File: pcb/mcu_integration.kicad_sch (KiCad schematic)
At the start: 32 parts, among them J5 DM3BT-DSF-PEJS, M1 MountingHole_Pad, M2 MountingHole_Pad, M3 MountingHole_Pad, M4 MountingHole_Pad, U1 STM32F103RBTx, U6 LM35DM, Y1 ECS-80-18-5PX-GM-TR

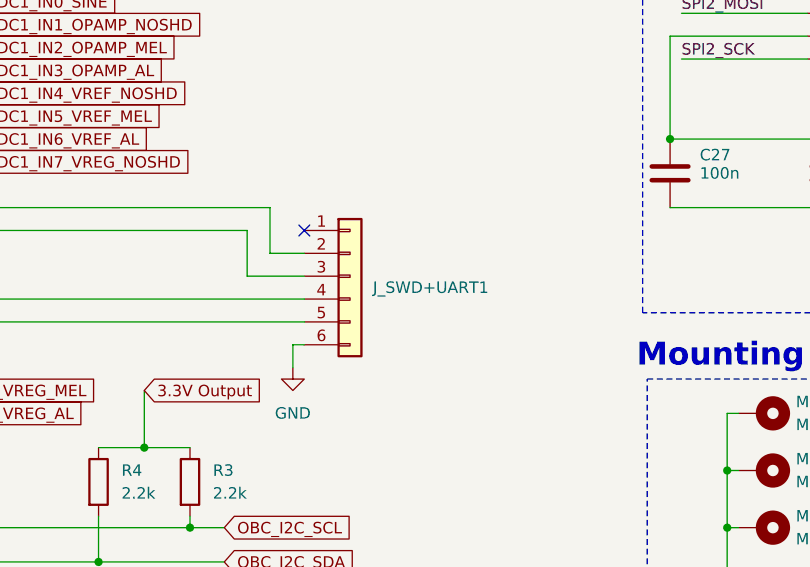
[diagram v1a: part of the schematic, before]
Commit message: Increased board size from 5x5 to 7x7
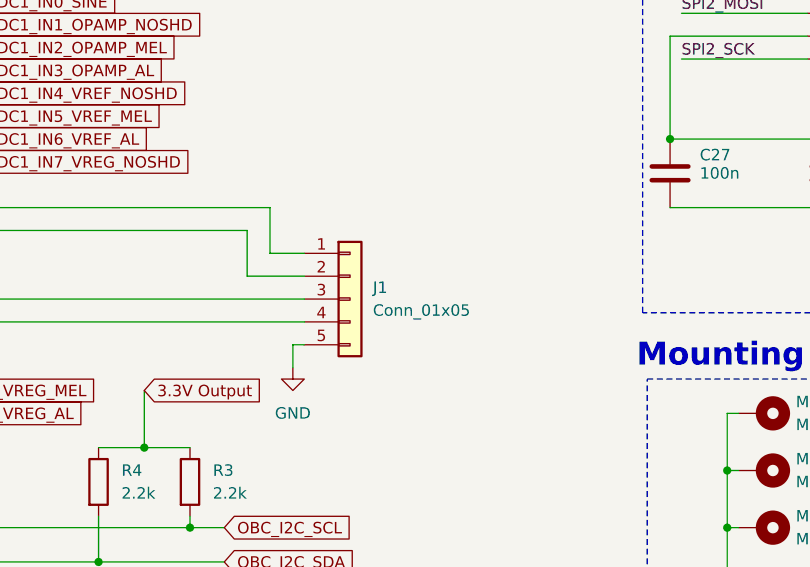
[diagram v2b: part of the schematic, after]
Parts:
- removed J_SWD+UART1: Conn_01x06, Connector_PinHeader_2.54mm:PinHeader_1x06_P2.54mm_Vertical, symbol Connector_Generic:Conn_01x06
- added J1: Conn_01x05, Connector_PinHeader_2.54mm:PinHeader_1x05_P2.54mm_Vertical, symbol Connector_Generic:Conn_01x05
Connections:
- net GND: now also J1.5 (Pin_5)
- net SWCLK: now also J1.4 (Pin_4)
- net SWDIO: now also J1.3 (Pin_3)
- net USART1_RX: now also J1.2 (Pin_2)
- net USART1_TX: now also J1.1 (Pin_1)
- no-connect marks 31 -> 30
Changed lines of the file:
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@@
 	)
 	(no_connect
-		(at 163.83 62.23)
-	)
-	(no_connect
 		(at 116.84 105.41)
 	)
@@
 	(label "SPI2_SCK"
 		(at 205.74 43.18 0)
+		(fields_autoplaced yes)
 		(effects
 			(font
@@
 	(label "SPI2_CS_NSS"
 		(at 205.74 35.56 0)
+		(fields_autoplaced yes)
 		(effects
 			(font
@@
 	(label "HSE_OSC_OUT"
 		(at 67.31 49.53 0)
+		(fields_autoplaced yes)
 		(effects
 			(font
@@
 	(label "USART1_TX"
 		(at 119.38 59.69 0)
+		(fields_autoplaced yes)
 		(effects
 			(font
@@
 	(label "HSE_OSC_IN"
 		(at 67.31 46.99 0)
+		(fields_autoplaced yes)
 		(effects
 			(font
@@
 	(label "SPI2_CS_NSS"
 		(at 119.38 110.49 0)
+		(fields_autoplaced yes)
 		(effects
 			(font
@@
 	(label "SPI2_MOSI"
 		(at 205.74 38.1 0)
+		(fields_autoplaced yes)
 		(effects
 			(font
@@
 	(label "SPI2_MOSI"
 		(at 119.38 118.11 0)
+		(fields_autoplaced yes)
 		(effects
 			(font
@@
 	(label "SPI2_MISO"
 		(at 119.38 115.57 0)
+		(fields_autoplaced yes)
 		(effects
 			(font
@@
 	(label "SWCLK"
 		(at 119.38 72.39 0)
+		(fields_autoplaced yes)
 		(effects
 			(font
@@
 	(label "USART1_RX"
 		(at 119.38 62.23 0)
+		(fields_autoplaced yes)
 		(effects
 			(font
@@
 	(label "SPI2_MISO"
 		(at 276.86 40.64 180)
+		(fields_autoplaced yes)
 		(effects
 			(font
@@
 	(label "BOOT0"
 		(at 68.58 40.64 0)
+		(fields_autoplaced yes)
 		(effects
 			(font
@@
 	(label "NRST"
 		(at 73.66 36.83 0)
+		(fields_autoplaced yes)
 		(effects
 			(font
@@
 	(label "SWDIO"
 		(at 119.38 69.85 0)
+		(fields_autoplaced yes)
 		(effects
 			(font
@@
 	(label "SPI2_SCK"
 		(at 119.38 113.03 0)
+		(fields_autoplaced yes)
 		(effects
 			(font
@@
 	)
 	(symbol
-		(lib_id "Connector_Generic:Conn_01x06")
-		(at 168.91 67.31 0)
-		(unit 1)
-		(exclude_from_sim no)
-		(in_bom yes)
-		(on_board yes)
-		(dnp no)
-		(fields_autoplaced yes)
-		(property "Reference" "J_SWD+UART1"
-			(at 171.45 68.58 0)
-			(effects
-				(font
-					(size 1.27 1.27)
-				)
-				(justify left)
-			)
-		)
-		(property "Value" "Conn_01x06"
-			(at 171.45 69.85 0)
-			(effects
-				(font
-					(size 1.27 1.27)
-				)
-				(justify left)
-				(hide yes)
-			)
-		)
-		(property "Footprint" "Connector_PinHeader_2.54mm:PinHeader_1x06_P2.54mm_Vertical"
-			(at 168.91 67.31 0)
-			(effects
-				(font
-					(size 1.27 1.27)
-				)
-				(hide yes)
-			)
-		)
-		(property "Datasheet" "~"
-			(at 168.91 67.31 0)
-			(effects
-				(font
-					(size 1.27 1.27)
-				)
-				(hide yes)
-			)
-		)
-		(property "Description" ""
-			(at 168.91 67.31 0)
-			(effects
-				(font
-					(size 1.27 1.27)
-				)
-				(hide yes)
-			)
-		)
-		(pin "1"
-		)
-		(pin "2"
-		)
-		(pin "3"
-		)
-		(pin "4"
-		)
-		(pin "5"
-		)
-		(pin "6"
-		)
-		(instances
-			(project "mcu_integration"
-				(path "/c0210bc3-f67f-47d8-a34e-f002a728adb2"
-					(reference "J_SWD+UART1")
-					(unit 1)
-				)
-			)
-		)
-	)
-	(symbol
 		(lib_id "Device:C")
 		(at 49.53 62.23 180)
@@
 					(unit 1)
 				)
+			)
+		)
+	)
+	(symbol
+		(lib_id "Connector_Generic:Conn_01x05")
+		(at 168.91 69.85 0)
+		(unit 1)
+		(exclude_from_sim no)
+		(in_bom yes)
+		(on_board yes)
+		(dnp no)
+		(fields_autoplaced yes)
+		(property "Reference" "J1"
+			(at 171.45 68.5799 0)
+			(effects
+				(font
+					(size 1.27 1.27)
+				)
+				(justify left)
+			)
+		)
+		(property "Value" "Conn_01x05"
+			(at 171.45 71.1199 0)
+			(effects
+				(font
+					(size 1.27 1.27)
+				)
+				(justify left)
+			)
+		)
+		(property "Footprint" "Connector_PinHeader_2.54mm:PinHeader_1x05_P2.54mm_Vertical"
+			(at 168.91 69.85 0)
+			(effects
+				(font
+					(size 1.27 1.27)
+				)
+				(hide yes)
+			)
+		)
+		(property "Datasheet" "~"
+			(at 168.91 69.85 0)
+			(effects
+				(font
+					(size 1.27 1.27)
+				)
+				(hide yes)
+			)
+		)
+		(property "Description" "Generic connector, single row, 01x05, script generated (kicad-library-utils/schlib/autogen/connector/)"
+			(at 168.91 69.85 0)
+			(effects
+				(font
+					(size 1.27 1.27)
+				)
+				(hide yes)
+			)
+		)
+		(pin "1"
+		)
+		(pin "4"
+		)
+		(pin "2"
+		)
+		(pin "5"
+		)
+		(pin "3"
+		)
+		(instances
+			(project ""
+				(path "/c0210bc3-f67f-47d8-a34e-f002a728adb2"
+					(reference "J1")
+					(unit 1)
+				)

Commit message: changed footprints and layout
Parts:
- C1: footprint Resistor_SMD:R_0402_1005Metric -> Capacitor_SMD:C_0402_1005Metric
- D2, D3: footprint Diode_SMD:D_0402_1005Metric -> capstone:SOD-323_1P7X1P25_ONS
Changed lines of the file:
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@@
 			)
 		)
-		(property "Footprint" "Resistor_SMD:R_0402_1005Metric"
+		(property "Footprint" "Capacitor_SMD:C_0402_1005Metric"
 			(at 40.3352 31.75 0)
 			(effects
@@
 			)
 		)
-		(property "Footprint" "Diode_SMD:D_0402_1005Metric"
+		(property "Footprint" "capstone:SOD-323_1P7X1P25_ONS"
 			(at 217.17 144.78 0)
 			(effects
@@
 			)
 		)
-		(property "Footprint" "Diode_SMD:D_0402_1005Metric"
+		(property "Footprint" "capstone:SOD-323_1P7X1P25_ONS"
 			(at 190.5 151.13 0)
 			(effects

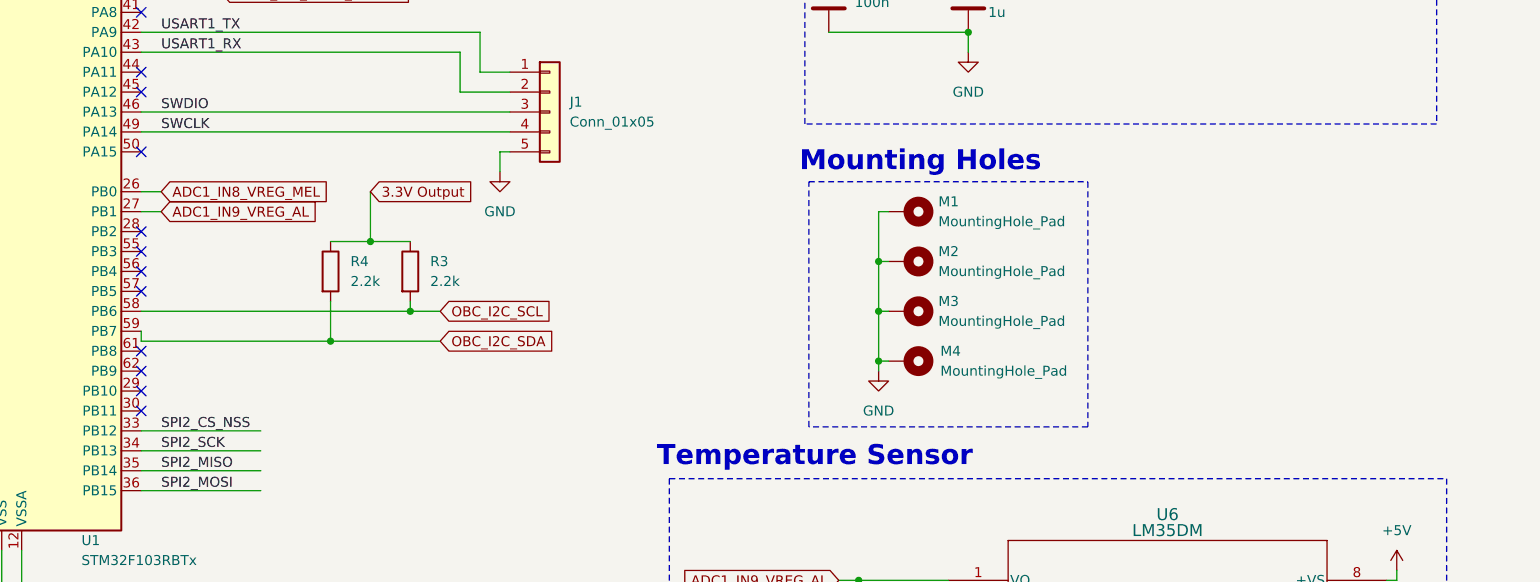
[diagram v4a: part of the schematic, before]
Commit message: Added Shields
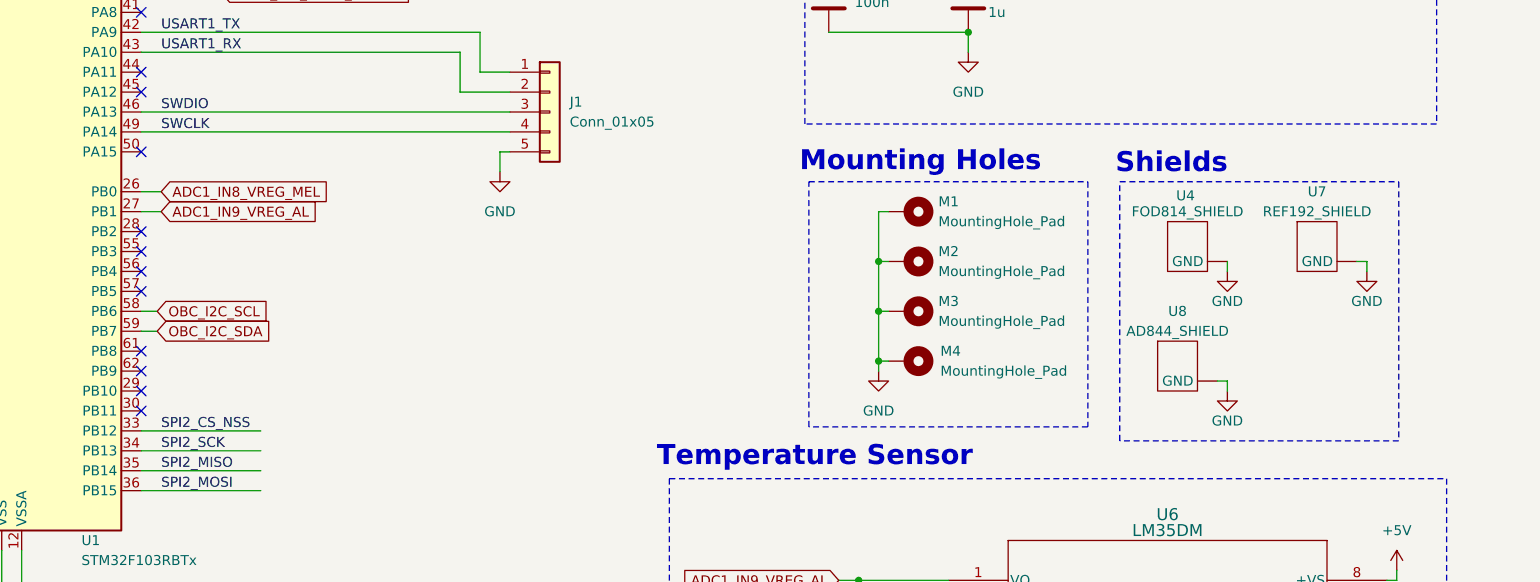
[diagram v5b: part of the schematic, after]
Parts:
- removed R3, R4: 2.2k, Resistor_SMD:R_0402_1005Metric, symbol Device:R
- added U4: FOD814_SHIELD, capstone:FOD814 Shield, symbol capstone:FOD814_SHIELD
- added U7: REF192_SHIELD, capstone:REF192 Shield, symbol capstone:REF192_SHIELD
- added U8: AD844_SHIELD, capstone:AD844 Shield, symbol capstone:AD844_SHIELD
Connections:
- net GND: now also U4. (GND), U7. (GND), U8. (GND)
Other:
- note added: "Shields"

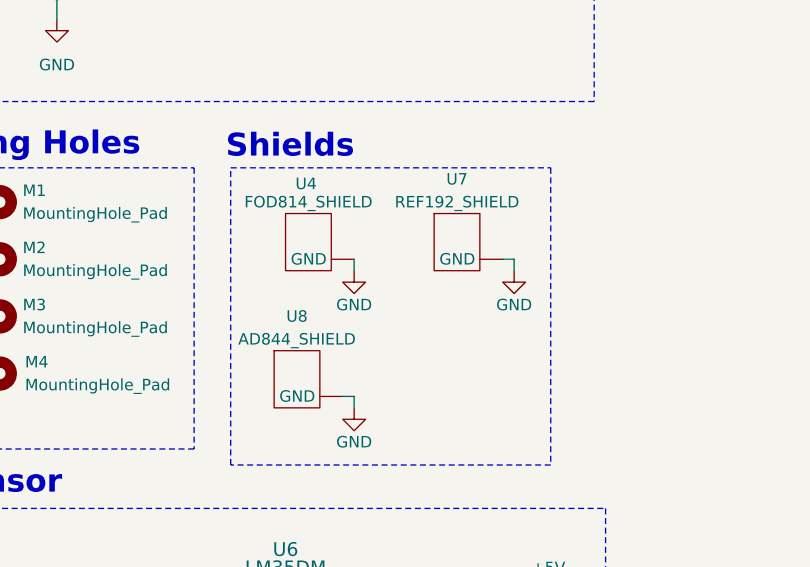
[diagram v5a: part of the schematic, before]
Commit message: Fixed Footprints
-Added Solder Mask
-Symbol Pin Numbers
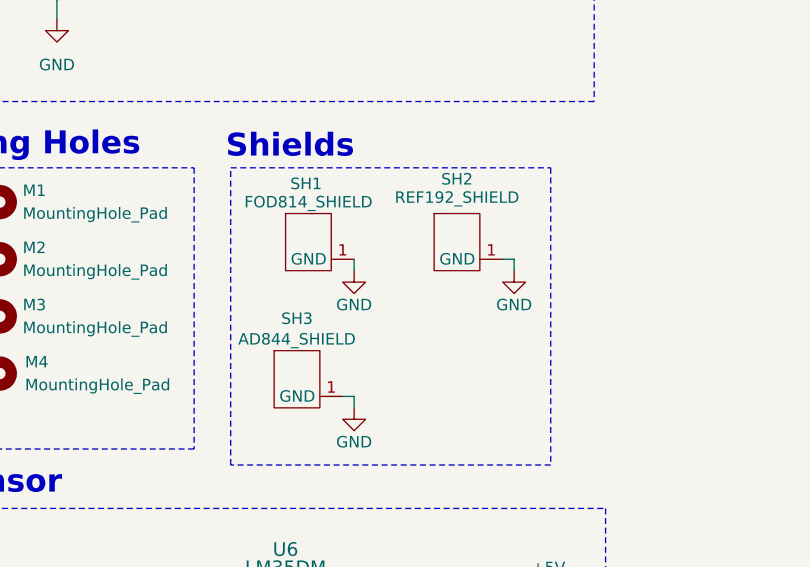
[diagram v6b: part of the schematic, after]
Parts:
- renumbered U4 to SH1, U7 to SH2, U8 to SH3
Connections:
- net GND: now also SH1.1 (GND), SH2.1 (GND), SH3.1 (GND); no longer SH1. (GND), SH2. (GND), SH3. (GND)
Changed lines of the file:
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@@
 		(on_board yes)
 		(dnp no)
-		(property "Reference" "U4"
+		(property "Reference" "SH1"
 			(at 249.936 80.518 0)
 			(effects
@@
 			)
 		)
-		(pin ""
+		(pin "1"
 		)
 		(instances
 			(project ""
 				(path "/c0210bc3-f67f-47d8-a34e-f002a728adb2"
-					(reference "U4")
+					(reference "SH1")
 					(unit 1)
 				)
@@
 		(on_board yes)
 		(dnp no)
-		(fields_autoplaced yes)
-		(property "Reference" "U7"
+		(property "Reference" "SH2"
 			(at 266.7 80.01 0)
 			(effects
@@
 		)
 		(property "Value" "REF192_SHIELD"
-			(at 266.7 82.55 0)
+			(at 266.7 82.042 0)
 			(effects
 				(font
@@
 			)
 		)
-		(pin ""
+		(pin "1"
 		)
 		(instances
 			(project ""
 				(path "/c0210bc3-f67f-47d8-a34e-f002a728adb2"
-					(reference "U7")
+					(reference "SH2")
 					(unit 1)
 				)
@@
 		(on_board yes)
 		(dnp no)
-		(fields_autoplaced yes)
-		(property "Reference" "U8"
-			(at 248.92 95.25 0)
+		(property "Reference" "SH3"
+			(at 248.92 95.504 0)
 			(effects
 				(font
@@
 			)
 		)
-		(pin ""
+		(pin "1"
 		)
 		(instances
 			(project ""
 				(path "/c0210bc3-f67f-47d8-a34e-f002a728adb2"
-					(reference "U8")
+					(reference "SH3")
 					(unit 1)
 				)
